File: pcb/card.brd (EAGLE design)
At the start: 69.5 x 40.6 mm, 23 parts, among them IC1 74HC14D, IC2 24LC256SN, Q1 BC817

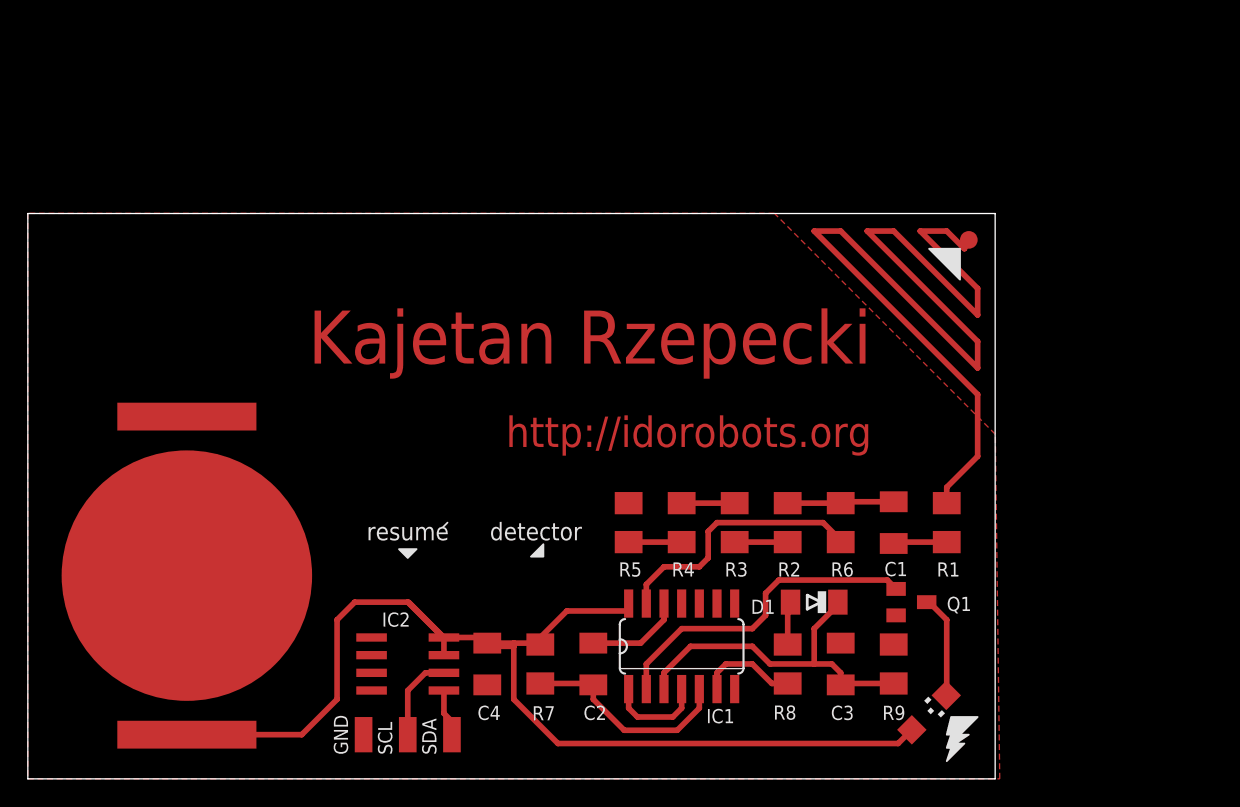
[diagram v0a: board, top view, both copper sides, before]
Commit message: Adjusted the PCB size & improved the design.
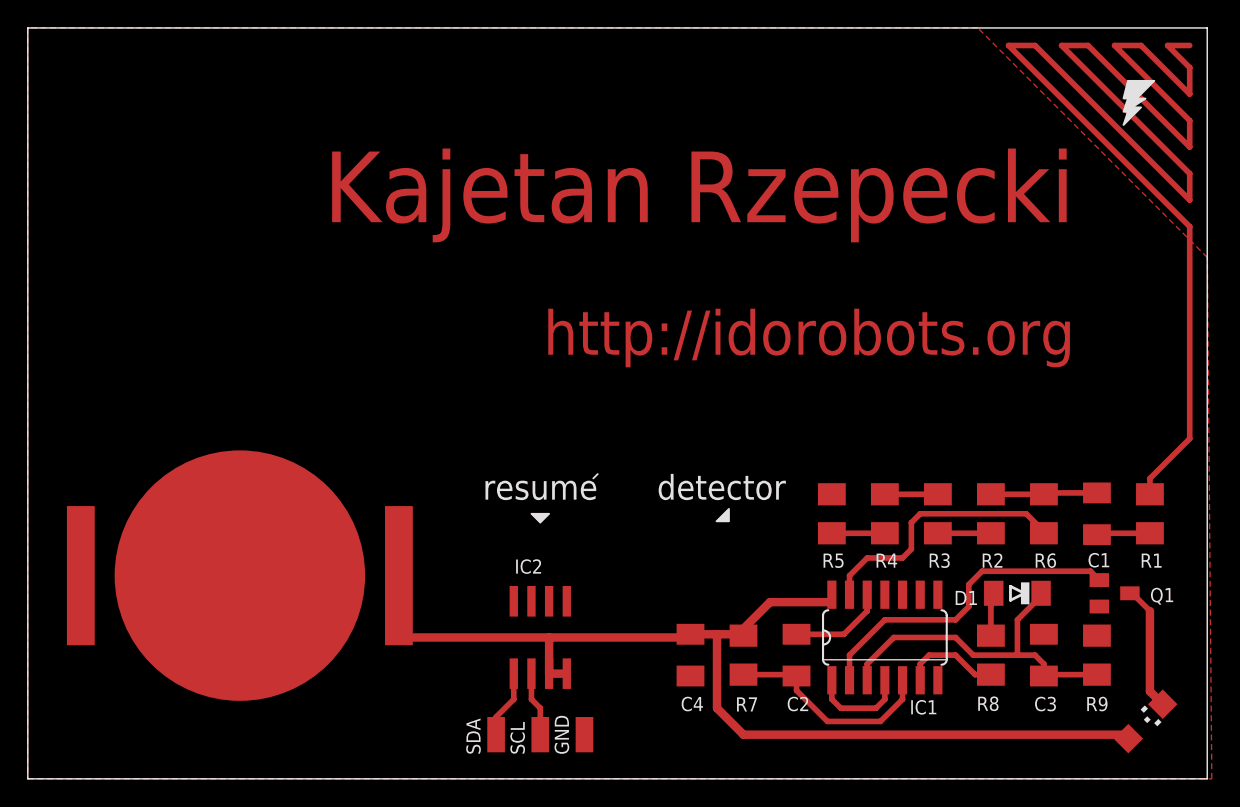
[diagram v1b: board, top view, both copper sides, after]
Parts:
- removed ANT: TPB1,27, testpad:B1,27
- moved GND 15.9 mm to (40.0, 3.17)
- moved LED 15.6 mm to (80.3, 4.13)
- moved C3 14.6 mm to (73.0, 8.89)
- moved D1 14.6 mm to (71.1, 13.3)
- moved Q1 14.6 mm to (78.1, 13.3)
- moved R2 14.6 mm to (69.2, 19.1)
- moved R3 14.6 mm to (65.4, 19.1)
- moved R6 14.6 mm to (73.0, 19.1)
- moved R7 14.6 mm to (51.4, 8.89)
- moved R8 14.6 mm to (69.2, 8.89)
- moved C1 14.6 mm to (76.8, 19.1)
- moved C2 14.6 mm to (55.2, 8.89)
- moved C4 14.6 mm to (47.6, 8.89)
- moved IC1 14.6 mm to (61.6, 10.2)
- moved R4 14.6 mm to (61.6, 19.1)
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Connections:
- net ANT: no longer ANT.TP
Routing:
- net ANT: track 76.9 -> 105.7 mm
- net VCC: track 85.1 -> 79.0 mm
- net N$9: track 6.30 -> 4.65 mm
- net N$13: track 7.41 -> 9.05 mm
- net N$10: track 3.41 -> 4.91 mm
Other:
- board size 69.5 x 40.6 mm -> 84.8 x 54 mm

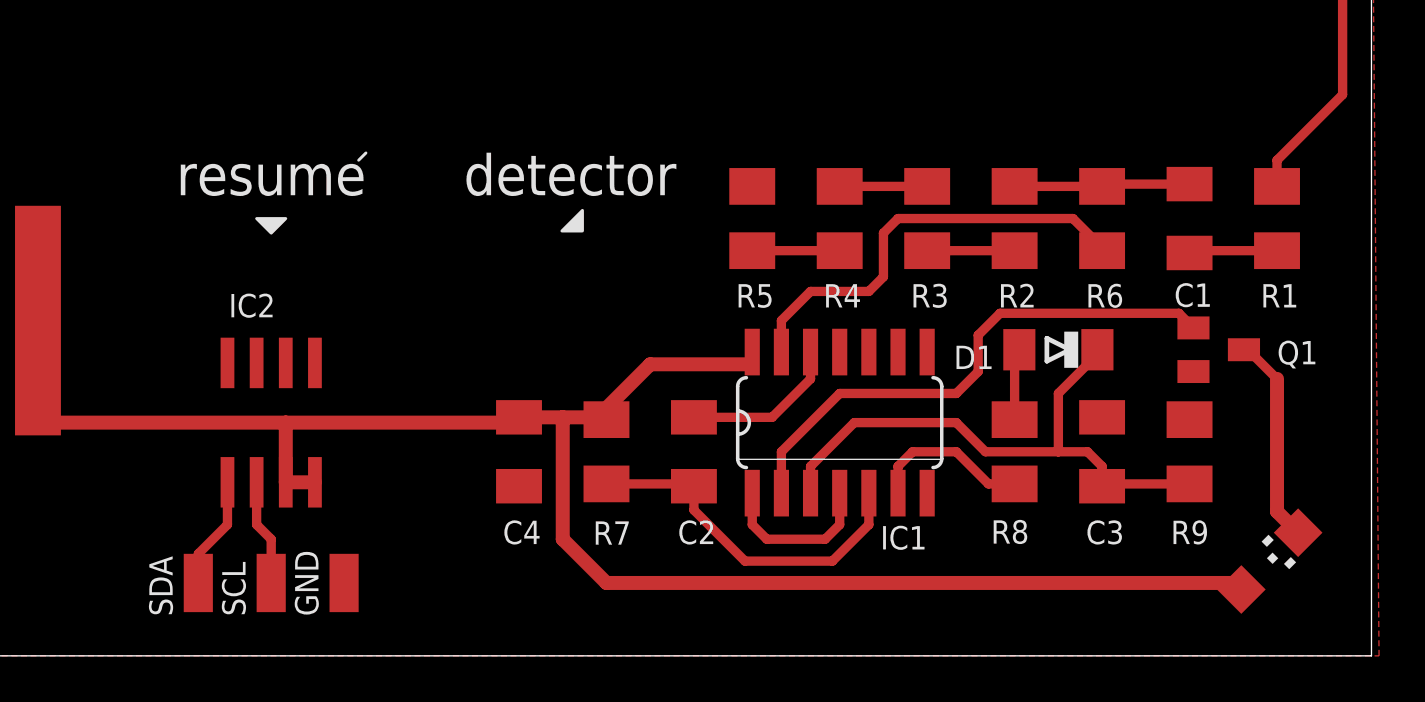
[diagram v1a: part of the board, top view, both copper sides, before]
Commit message: Adjusted the soldermask expantion on the top layer text.
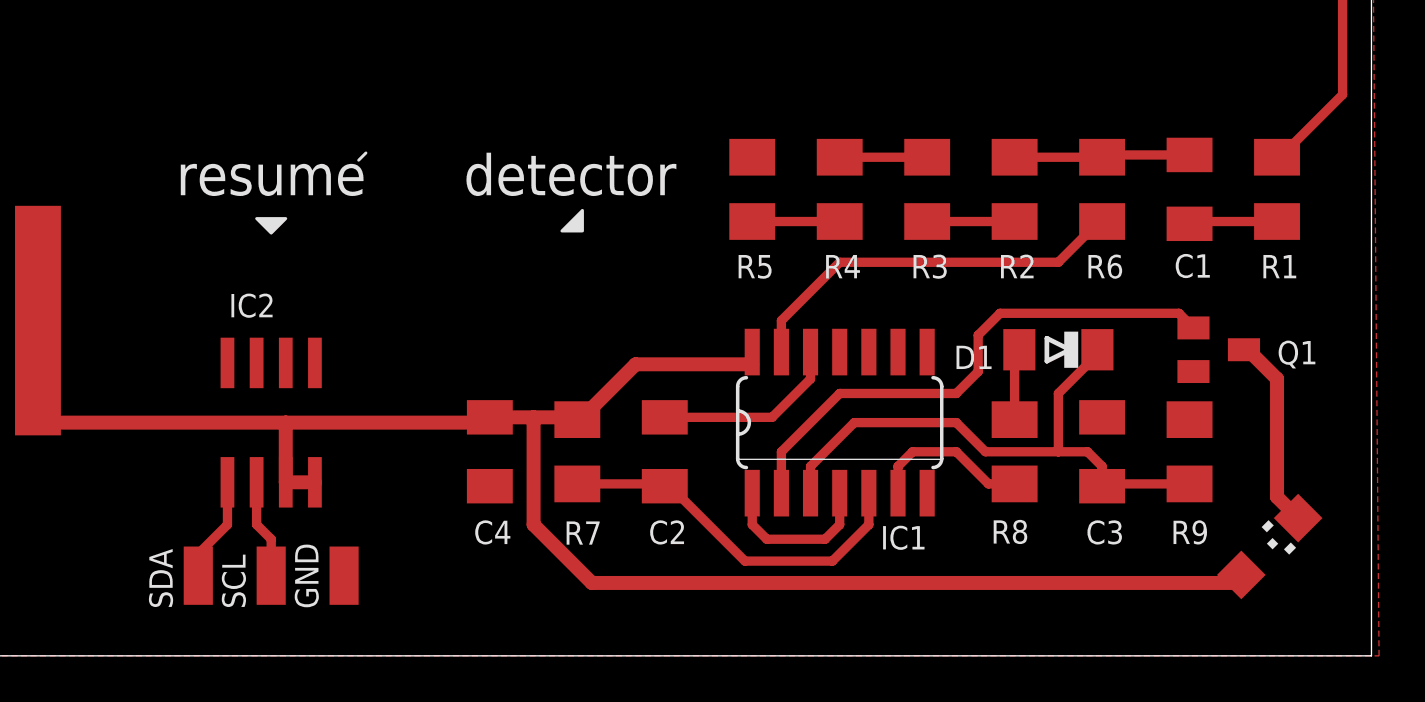
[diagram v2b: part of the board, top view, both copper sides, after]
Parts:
- moved C4 1.27 mm to (46.4, 8.89)
- moved R7 1.27 mm to (50.2, 8.89)
- moved C1 1.27 mm to (76.8, 20.3)
- moved R1 1.27 mm to (80.6, 20.3)
- moved R2 1.27 mm to (69.2, 20.3)
- moved R3 1.27 mm to (65.4, 20.3)
- moved R4 1.27 mm to (61.6, 20.3)
- moved R5 1.27 mm to (57.8, 20.3)
- moved R6 1.27 mm to (73.0, 20.3)
- moved C2 1.27 mm to (54.0, 8.89)
- moved LED 0.63 mm to (80.3, 4.76)
- moved GND 0.32 mm to (40.0, 3.49)
- moved SCL 0.32 mm to (36.8, 3.49)
- moved SDA 0.32 mm to (33.7, 3.49)
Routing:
- net N$3: track 19.9 -> 17.1 mm
- net N$4: track 6.94 -> 8.21 mm
- net VCC: track 79.0 -> 80.0 mm
- net ANT: track 105.7 -> 104.7 mm
- net N$5: track 16.0 -> 17.0 mm
- net N$13: track 9.05 -> 8.41 mm

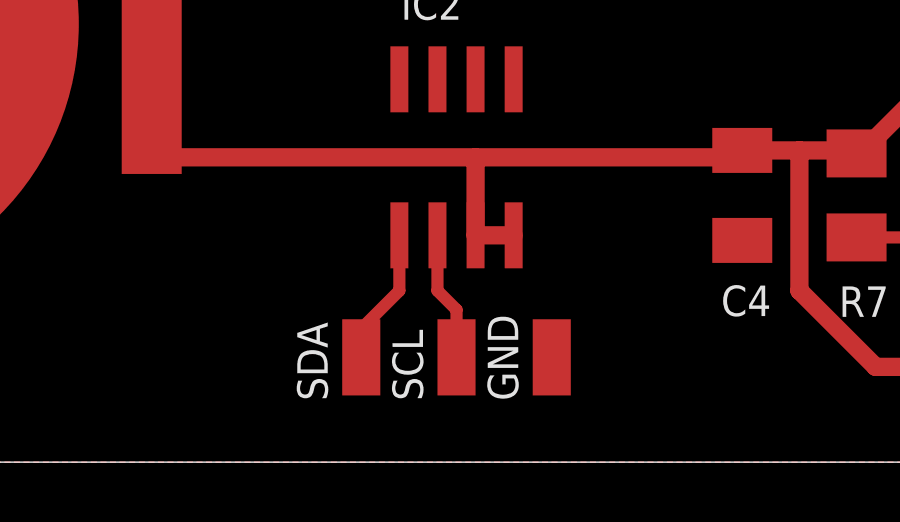
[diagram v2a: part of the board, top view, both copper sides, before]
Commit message: Reduced spacing and changed the shape of resume testpads.
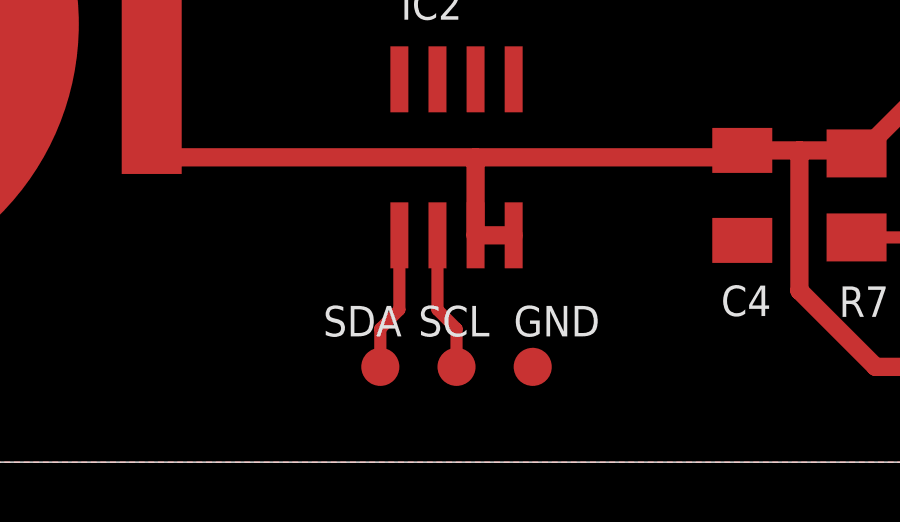
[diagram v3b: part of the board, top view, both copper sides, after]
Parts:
- GND, SCL, SDA: value (none) -> TPB1,27; device wirepad:SMD1,27-2,54 -> testpad:B1,27
- moved GND 0.71 mm to (39.4, 3.17), turned to 0 degrees
- moved SDA 0.71 mm to (34.3, 3.17), turned to 0 degrees
- moved SCL 0.32 mm to (36.8, 3.17), turned to 0 degrees
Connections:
- net GND: now also GND.TP; no longer GND.1
- net N$10: now also SDA.TP; no longer SDA.1
- net N$9: now also SCL.TP; no longer SCL.1
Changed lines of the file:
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@@
 <attribute name="NAME" x="51.245009375" y="5.857546875" size="1.016" layer="25" rot="R180"/>
-</element>
-<element name="SDA" library="wirepad" package="SMD1,27-2,54" value="" x="33.655" y="3.4925" smashed="yes" rot="R180">
-<attribute name="VALUE" x="33.655" y="3.4925" size="0.0254" layer="27" rot="R180"/>
-<attribute name="NAME" x="32.5375" y="2.045" size="1.016" layer="25" rot="R90"/>
-</element>
-<element name="SCL" library="wirepad" package="SMD1,27-2,54" value="" x="36.83" y="3.4925" smashed="yes" rot="R180">
-<attribute name="VALUE" x="36.83" y="3.4925" size="0.0254" layer="27" rot="R180"/>
-<attribute name="NAME" x="35.7125" y="2.045" size="1.016" layer="25" rot="R90"/>
 </element>
 <element name="IC2" library="microchip" package="SO-08" value="24LC256SN" x="36.83" y="10.16" smashed="yes" rot="R180">
@@
 <attribute name="NAME" x="34.972496875" y="14.747109375" size="1.016" layer="25"/>
 </element>
-<element name="GND" library="wirepad" package="SMD1,27-2,54" value="" x="40.005" y="3.4925" smashed="yes" rot="R180">
-<attribute name="VALUE" x="40.005" y="3.4925" size="0.0254" layer="27" rot="R180"/>
-<attribute name="NAME" x="38.8875" y="2.045" size="1.016" layer="25" rot="R90"/>
-</element>
 <element name="C1" library="resistor" package="C1206K" value="10nF" x="76.835" y="20.32" smashed="yes" rot="R90">
 <attribute name="NAME" x="77.83510625" y="17.4906" size="1.016" layer="25" rot="R180"/>
@@
 </element>
 <element name="BAT" library="bat" package="KB3003" value="KB3003" x="15.24" y="14.605"/>
+<element name="SCL" library="testpad" package="B1,27" value="TPB1,27" x="36.83" y="3.175" smashed="yes">
+<attribute name="TP_SIGNAL_NAME" value="" x="36.195" y="1.27" size="1" layer="37"/>
+<attribute name="NAME" x="35.56" y="4.191" size="1.016" layer="25" ratio="10"/>
+</element>
+<element name="GND" library="testpad" package="B1,27" value="TPB1,27" x="39.37" y="3.175" smashed="yes">
+<attribute name="TP_SIGNAL_NAME" value="" x="38.735" y="1.27" size="1" layer="37"/>
+<attribute name="NAME" x="38.735" y="4.191" size="1.016" layer="25" ratio="10"/>
+</element>
+<element name="SDA" library="testpad" package="B1,27" value="TPB1,27" x="34.29" y="3.175" smashed="yes">
+<attribute name="TP_SIGNAL_NAME" value="" x="33.655" y="1.27" size="1" layer="37"/>
+<attribute name="NAME" x="32.385" y="4.191" size="1.016" layer="25" ratio="10"/>
+</element>
 </elements>
 <signals>
@@
 <contactref element="IC2" pad="3"/>
 <contactref element="IC2" pad="4"/>
-<contactref element="GND" pad="1"/>
 <contactref element="R5" pad="1"/>
 <contactref element="BAT" pad="-"/>
+<contactref element="GND" pad="TP"/>
 </signal>
 <signal name="VCC">
@@
 </signal>
 <signal name="N$9">
-<contactref element="SCL" pad="1"/>
 <contactref element="IC2" pad="6"/>
-<wire x1="36.195" y1="7.56" x2="36.195" y2="5.715" width="0.4064" layer="1"/>
-<wire x1="36.195" y1="5.715" x2="36.83" y2="5.08" width="0.4064" layer="1"/>
-<wire x1="36.83" y1="5.08" x2="36.83" y2="3.4925" width="0.4064" layer="1"/>
+<contactref element="SCL" pad="TP"/>
+<wire x1="36.195" y1="7.56" x2="36.195" y2="5.08" width="0.4064" layer="1"/>
+<wire x1="36.195" y1="5.08" x2="36.83" y2="4.445" width="0.4064" layer="1"/>
+<wire x1="36.83" y1="4.445" x2="36.83" y2="3.175" width="0.4064" layer="1"/>
 </signal>
 <signal name="N$10">
-<contactref element="SDA" pad="1"/>
 <contactref element="IC2" pad="5"/>
-<wire x1="34.925" y1="7.56" x2="34.925" y2="5.715" width="0.4064" layer="1"/>
-<wire x1="34.925" y1="5.715" x2="33.655" y2="4.445" width="0.4064" layer="1"/>
-<wire x1="33.655" y1="4.445" x2="33.655" y2="3.4925" width="0.4064" layer="1"/>
+<contactref element="SDA" pad="TP"/>
+<wire x1="34.925" y1="7.56" x2="34.925" y2="5.08" width="0.4064" layer="1"/>
+<wire x1="34.925" y1="5.08" x2="34.29" y2="4.445" width="0.4064" layer="1"/>
+<wire x1="34.29" y1="4.445" x2="34.29" y2="3.175" width="0.4064" layer="1"/>
 </signal>
 <signal name="ANT">
